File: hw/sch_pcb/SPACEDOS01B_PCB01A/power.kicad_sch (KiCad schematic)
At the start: 15 parts, among them J1 HEADER_2x01, J2 HEADER_2x01_PARALLEL, J3 HEADER_2x01_PARALLEL, U8 TPS613222ADBV

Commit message: Update designs to KiCAD 6. Update schematics datasheet links Minor schematics improvements (titleblocks, schematics layout)
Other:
- company: (none) -> www.ust.cz
- title: (none) -> SPACEDOS01B
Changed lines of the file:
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@@
 (kicad_sch (version 20211123) (generator eeschema)
   (paper "A4")
+  (title_block
+    (title "SPACEDOS01B")
+    (date "2023-01-26")
+    (company "www.ust.cz")
+    (comment 1 "Semiconductor \\nIonizing radiation \\nsatellite spectrometer  \\nand dosimeter ")
+    (comment 3 "Universal Scientific Technologies s.r.o. ")
+  )
   (junction (at 157.48 83.82) (diameter 0) (color 0 0 0 0)
   )
@@
       (effects (font (size 1.524 1.524)) hide)
     )
-    (property "Datasheet" "" (id 3) (at 185.42 86.36 0)
-      (effects (font (size 1.524 1.524)) hide)
-    )
+    (property "Datasheet" "https://www.ti.com/lit/ds/symlink/tps61322.pdf" (id 3) (at 185.42 86.36 0)
+      (effects (font (size 1.524 1.524)) hide)
+    )

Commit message: Correcly setup automation workflows and cleanup KiCAD project.
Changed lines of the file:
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@@
   (junction (at 237.49 83.82) (diameter 0) (color 0 0 0 0)
   )
+  (junction (at 50.8 68.58) (diameter 0) (color 0 0 0 0)
+  )
   (junction (at 213.36 83.82) (diameter 0) (color 0 0 0 0)
   )
@@
   )
   (junction (at 97.79 85.09) (diameter 0) (color 0 0 0 0)
+  )
+  (junction (at 109.22 85.09) (diameter 0) (color 0 0 0 0)
   )
   (junction (at 71.12 85.09) (diameter 0) (color 0 0 0 0)
@@
     (stroke (width 0) (type default) (color 0 0 0 0))
   )
+  (wire (pts (xy 109.22 85.09) (xy 111.125 85.09))
+    (stroke (width 0) (type default) (color 0 0 0 0))
+  )
   (wire (pts (xy 78.74 93.98) (xy 78.74 95.25))
     (stroke (width 0) (type default) (color 0 0 0 0))
@@
     (stroke (width 0) (type default) (color 0 0 0 0))
   )
+  (wire (pts (xy 50.8 68.58) (xy 52.705 68.58))
+    (stroke (width 0) (type default) (color 0 0 0 0))
+  )
   (wire (pts (xy 109.22 85.09) (xy 109.22 72.39))
+    (stroke (width 0) (type default) (color 0 0 0 0))
+  )
+  (wire (pts (xy 237.49 83.82) (xy 239.395 83.82))
     (stroke (width 0) (type default) (color 0 0 0 0))
   )
@@
     (pin "2")
   )
+  (symbol (lib_id "power:PWR_FLAG") (at 111.125 85.09 270) (unit 1)
+    (in_bom yes) (on_board yes)
+    (property "Reference" "#FLG0102" (id 0) (at 113.03 85.09 0)
+      (effects (font (size 1.27 1.27)) hide)
+    )
+    (property "Value" "PWR_FLAG" (id 1) (at 114.935 85.09 0))
+    (property "Footprint" "" (id 2) (at 111.125 85.09 0)
+      (effects (font (size 1.27 1.27)) hide)
+    )
+    (property "Datasheet" "~" (id 3) (at 111.125 85.09 0)
+      (effects (font (size 1.27 1.27)) hide)
+    )
+    (pin "1")
+  )
+  (symbol (lib_id "power:PWR_FLAG") (at 239.395 83.82 270) (unit 1)
+    (in_bom yes) (on_board yes) (fields_autoplaced)
+    (property "Reference" "#FLG0105" (id 0) (at 241.3 83.82 0)
+      (effects (font (size 1.27 1.27)) hide)
+    )
+    (property "Value" "PWR_FLAG" (id 1) (at 242.57 84.2538 90)
+      (effects (font (size 1.27 1.27)) (justify left))
+    )
+    (property "Footprint" "" (id 2) (at 239.395 83.82 0)
+      (effects (font (size 1.27 1.27)) hide)
+    )
+    (property "Datasheet" "~" (id 3) (at 239.395 83.82 0)
+      (effects (font (size 1.27 1.27)) hide)
+    )
+    (pin "1")
+  )
+  (symbol (lib_id "power:PWR_FLAG") (at 52.705 68.58 270) (unit 1)
+    (in_bom yes) (on_board yes)
+    (property "Reference" "#FLG0101" (id 0) (at 54.61 68.58 0)
+      (effects (font (size 1.27 1.27)) hide)
+    )
+    (property "Value" "PWR_FLAG" (id 1) (at 56.515 68.58 0))
+    (property "Footprint" "" (id 2) (at 52.705 68.58 0)
+      (effects (font (size 1.27 1.27)) hide)
+    )
+    (property "Datasheet" "~" (id 3) (at 52.705 68.58 0)
+      (effects (font (size 1.27 1.27)) hide)
+    )
+    (pin "1")
+  )
 )

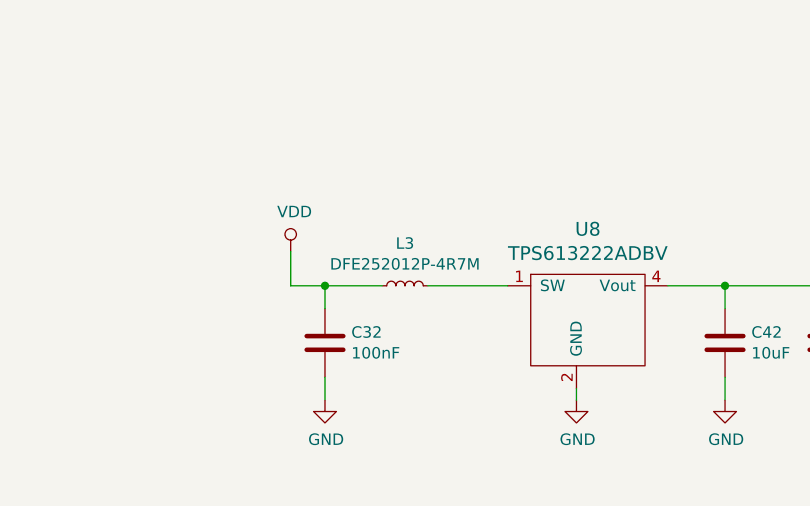
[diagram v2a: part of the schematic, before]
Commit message: Center PCB in page. Improve dimensions.
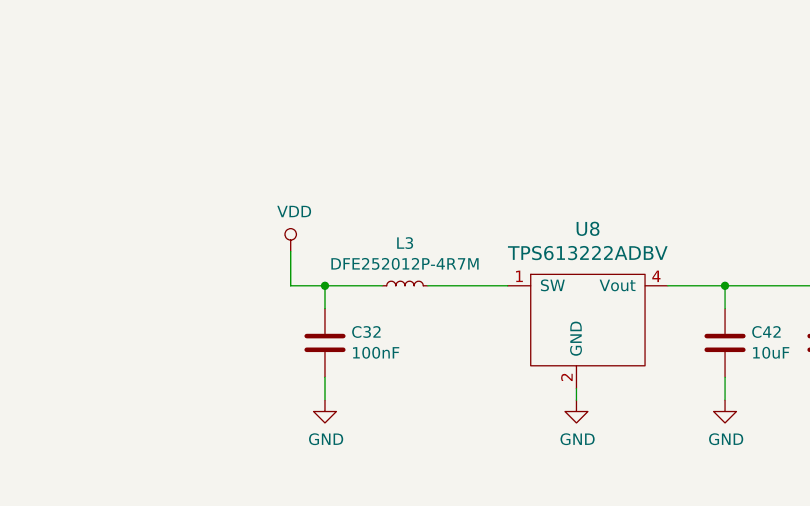
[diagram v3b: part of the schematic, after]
